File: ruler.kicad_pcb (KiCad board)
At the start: 2 copper layers, 170.8 x 38.1 mm, 63 parts, among them J1 USB_OTG, Q1 SOT23, Q2 SOT323, Q3 SOT883, Q4 SOT523, Q5 SOT223, SW1 KMR2, SW2 EVQPE1, SW3 B3U1000P, SW4 FSMCT, SW5 TL3315, SW6 FSM2JSM, SW7 JS202011SCQN, U1 QFN-0.5mm, U2 LQFP, U3 SOIC, U4 BGA-0.8mm, U5 TSSOP-0.65mm, U6 MSOIC, U7 TSOP-0.95mm

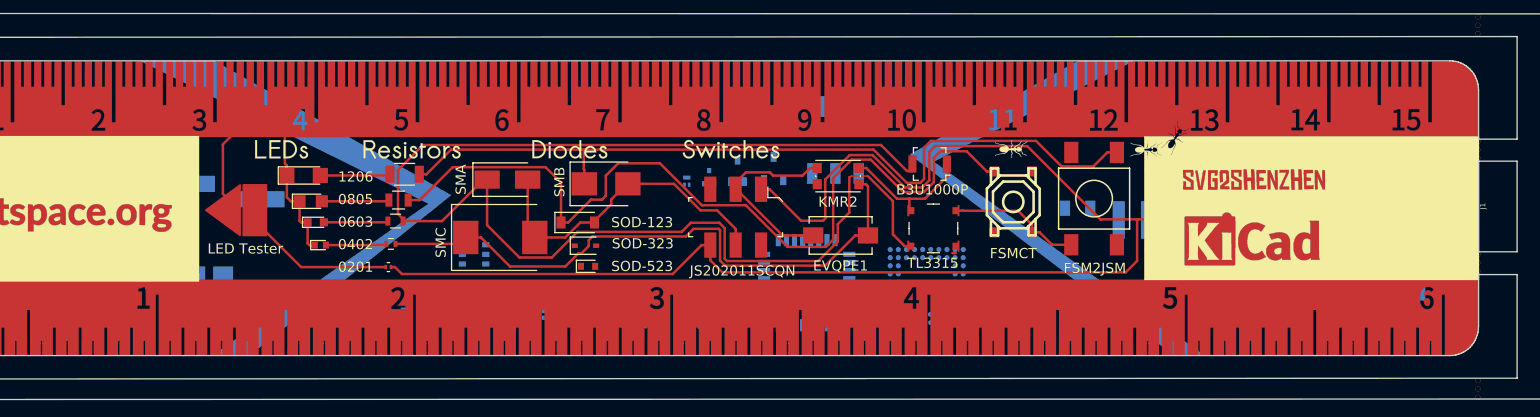
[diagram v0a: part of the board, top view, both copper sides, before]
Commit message: Adjust inductors
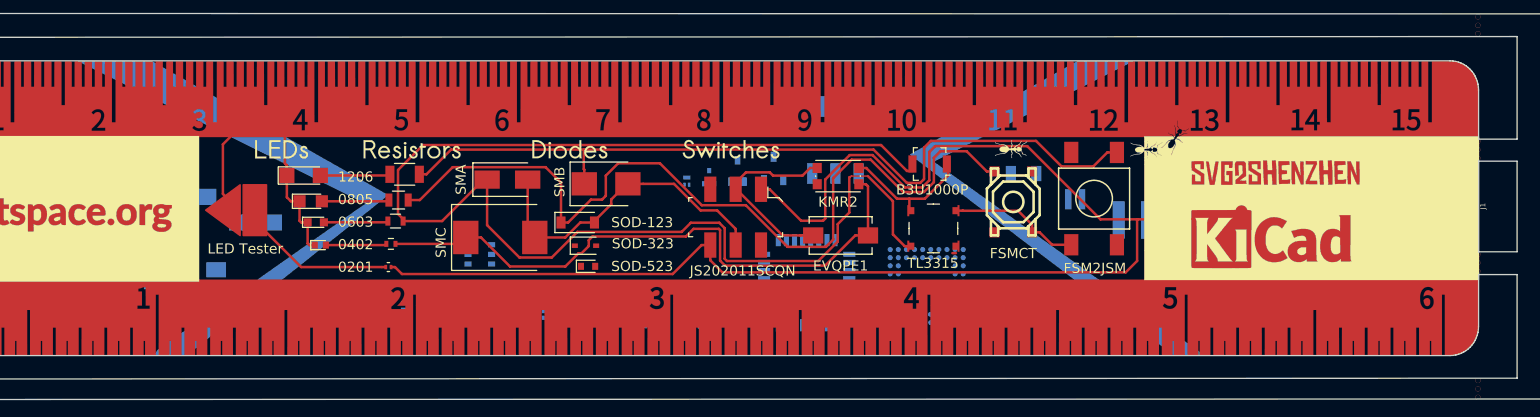
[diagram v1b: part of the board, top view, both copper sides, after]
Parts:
- added L6: 2x2mm, KiCad/Inductors.pretty:Inductor_Taiyo-Yuden_NR-20xx, B.Cu at (184.7, 104.1)
- L2: value SRU8043 -> 8x8mm; footprint custom:Inductor_Bourns-SRU8043 -> KiCad/Inductors.pretty:Inductor_Taiyo-Yuden_NR-80xx
- L3: value 4040 -> 4x4mm
- L4: value 5050 -> 5x5mm
- L5: value 60xx -> 6x6mm
- moved L1 6.34 mm to (179.6, 101.6)
- moved DRAWING6 4.07 mm to (73.4, 92.7)
- moved C1 2.30 mm to (103.9, 106.4)
- moved C2 1.29 mm to (96.9, 103.9)
- moved C5 0.81 mm to (98.6, 111.1)
- moved DRAWING8 0.80 mm to (141.0, 111.0)
- moved DRAWING12 0.76 mm to (65.3, 98.0)
- moved U7 0.56 mm to (126.0, 109.6)
- moved C3 0.42 mm to (88.6, 101.7)
- moved C6 0.13 mm to (92.3, 111.8)

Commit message: A lot of changes
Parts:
- removed DRAWING7: Conn_01x01, drawings:transistors_text
- removed DRAWING8: Conn_01x01, drawings:ics_text
- added DRAWING15: Conn_01x01, drawings:chipmunk, B.Cu at (202.7, 96.5)
- added DRAWING16: Conn_01x01, drawings:weasel, B.Cu at (214.4, 98.6)
- added DRAWING17: Conn_01x01, drawings:ant, B.Cu at (109.0, 120.9)
- added DRAWING18: Conn_01x01, drawings:ant, B.Cu at (177.5, 90.4)
- added Q6: SOT89, KiCad/TO_SOT_Packages_SMD.pretty:SOT-89-3, B.Cu at (154.7, 100.5)
- added Q7: SuperSOT, KiCad/TO_SOT_Packages_SMD.pretty:SuperSOT-3, B.Cu at (150.1, 100.9)
- added U10: SOT963-6, KiCad/TO_SOT_Packages_SMD.pretty:SOT-963, B.Cu at (119.4, 100.3)
- added U11: SSOP14, KiCad/SMD_Packages.pretty:SSOP-14, B.Cu at (178.8, 114.8)
- added U12: SO16-L, KiCad/SMD_Packages.pretty:SO-16-L, B.Cu at (126.2, 109.7)
- added U13: SOT666, KiCad/TO_SOT_Packages_SMD.pretty:SOT-666, B.Cu at (122.4, 100.1)
- added U14: SOT1194, adamgreig/agg-kicad/agg.pretty:SOT-1194-1, B.Cu at (168.1, 92.5)
- added U15: SOT1333, KiCad/TO_SOT_Packages_SMD.pretty:SOT-1333-1, B.Cu at (126.0, 99.8)
- added U16: SOT669, KiCad/TO_SOT_Packages_SMD.pretty:SOT-669_LFPAK, B.Cu at (114.3, 94.7)
- added U17: TSSOP 4.4x3mm, KiCad/Housings_SSOP.pretty:TSSOP-8_4.4x3mm_Pitch0.65mm, B.Cu at (114.8, 116.1)
- added U18: SO4, KiCad/Housings_SOIC.pretty:SO-4_4.4x2.3mm_Pitch1.27mm, B.Cu at (142.7, 105.2)
- added U19: VSSOP, KiCad/Housings_SSOP.pretty:VSSOP-8_2.3x2mm_Pitch0.5mm, B.Cu at (168.1, 104.6)
- added U8: SOT23-6, KiCad/TO_SOT_Packages_SMD.pretty:SOT-23-6, B.Cu at (134.6, 99.6)
- added U9: SOT23-8, KiCad/TO_SOT_Packages_SMD.pretty:SOT-23-8, B.Cu at (130.0, 99.6)
- U5: value TSSOP-0.65mm -> TSSOP 3x3mm
- moved U7 23.4 mm to (149.4, 108.7)
- moved U6 9.38 mm to (137.2, 108.5)
- moved Q1 8.64 mm to (146.3, 101.1)
- moved Q3 8.39 mm to (138.0, 102.1)
- moved Q4 8.38 mm to (140.2, 102.4)
- moved Q2 8.38 mm to (143.0, 101.2)
- moved U5 7.63 mm to (115.8, 109.7)
- moved DRAWING14 6.78 mm to (188.7, 100.8)
- moved DRAWING13 3.62 mm to (213.4, 93.7)
- moved U3 1.83 mm to (137.2, 114.8)
- moved U2 1.39 mm to (158.5, 111.0)
- moved L1 0.92 mm to (180.3, 102.1)
- moved Q5 0.76 mm to (161.8, 98.3)
- moved U4 0.63 mm to (169.4, 112.5)
- moved U1 0.36 mm to (148.1, 114.8)
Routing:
- net GND: track 35.9 -> 33.8 mm

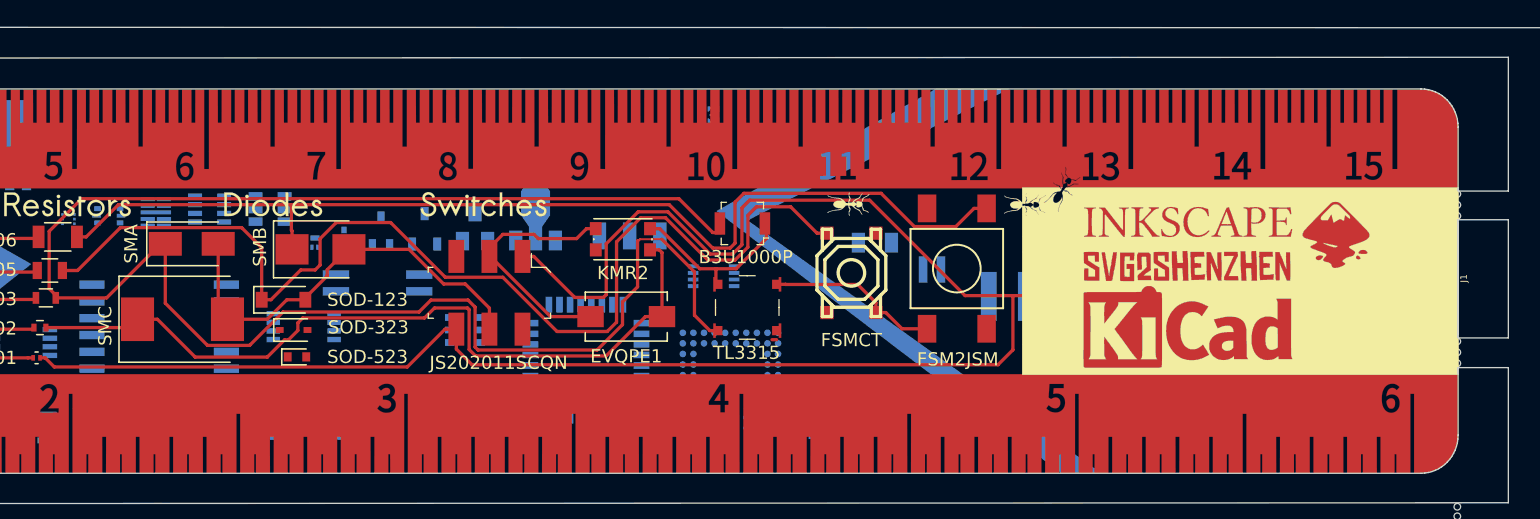
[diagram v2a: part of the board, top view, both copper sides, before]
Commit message: Adjust mouse-bite drills and plot
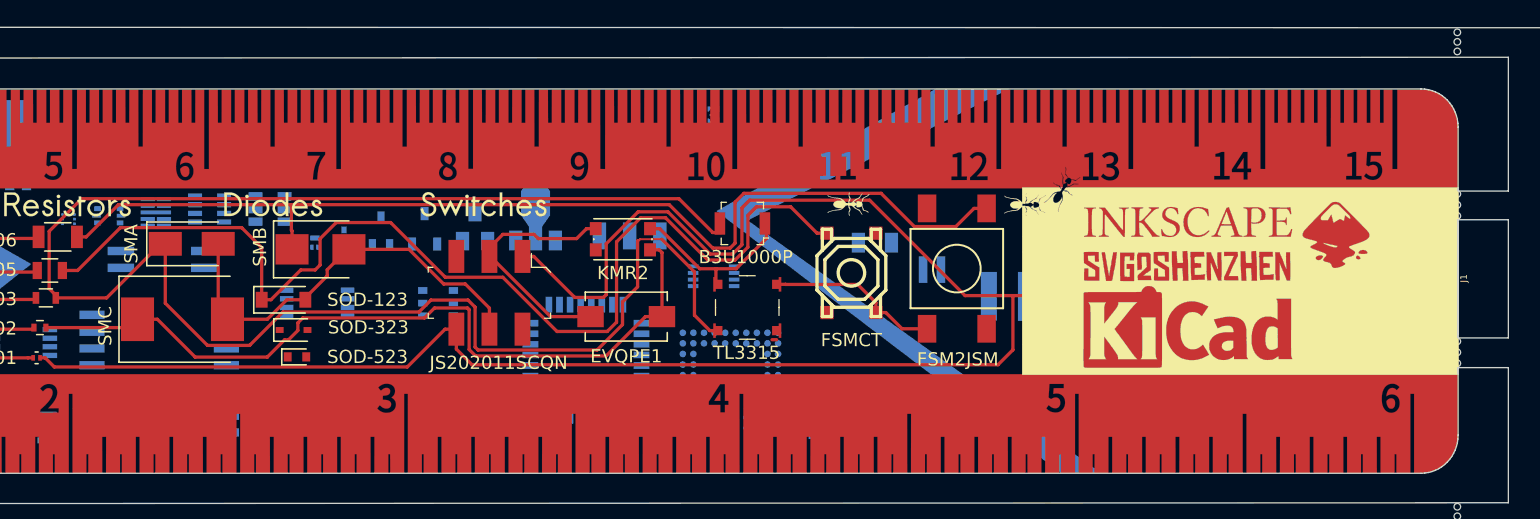
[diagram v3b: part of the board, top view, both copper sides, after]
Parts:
- moved U18 16.4 mm to (126.5, 103.4)
- moved U7 2.87 mm to (147.3, 106.7)
- moved U12 2.29 mm to (126.2, 112.0)
- moved U6 2.05 mm to (138.2, 106.7)
- moved U3 1.55 mm to (138.7, 114.6)

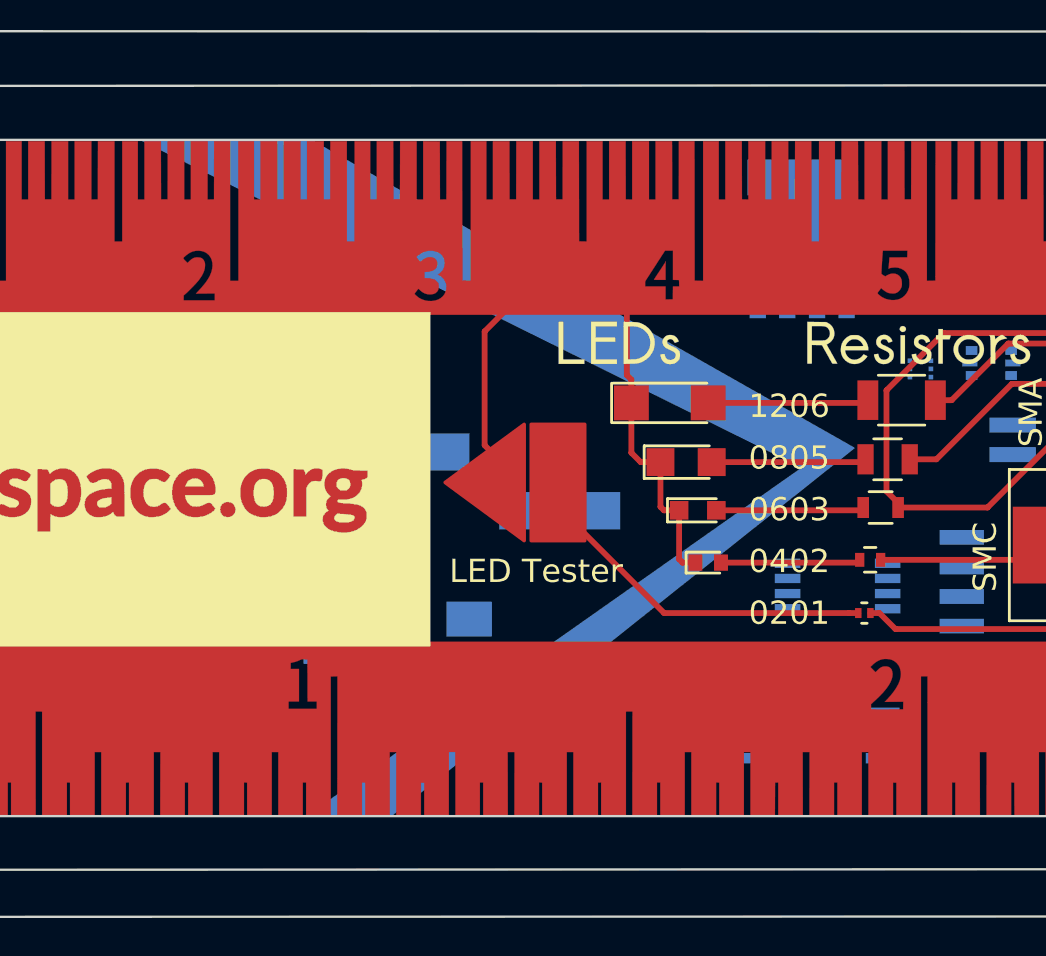
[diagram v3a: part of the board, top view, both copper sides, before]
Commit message: Adjust bottom separator graphics
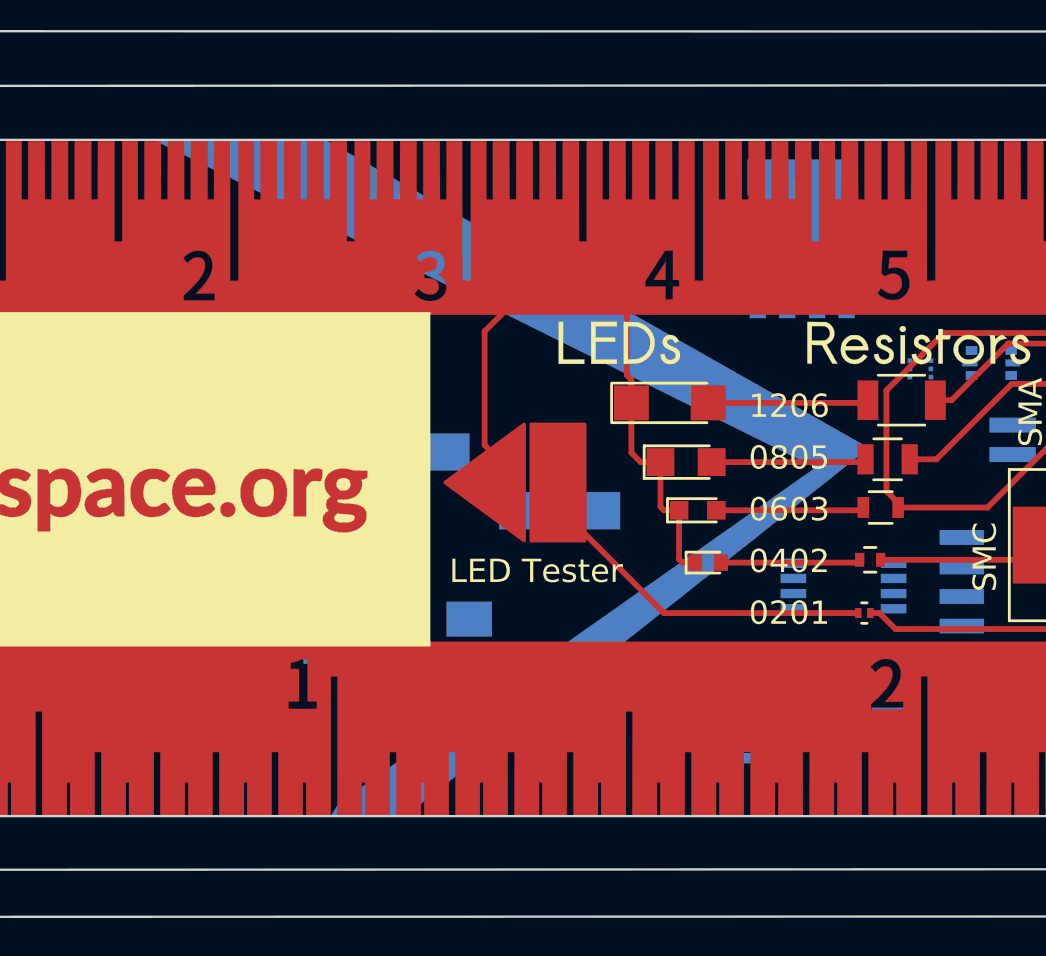
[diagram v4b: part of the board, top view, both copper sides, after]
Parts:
- moved U5 0.25 mm to (116.1, 109.7)
- moved U17 0.25 mm to (115.1, 116.1)
